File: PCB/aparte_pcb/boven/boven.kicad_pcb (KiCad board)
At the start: 2 copper layers, 100.5 x 100.5 mm, 48 parts, among them IC1 TSSP4038, IC10 TSSP4038, IC11 TSSP4038, IC12 TSSP4038, IC13 TSSP4038, IC14 TSSP4038, IC15 TSSP4038, IC16 TSSP4038, IC2 TSSP4038, IC3 TSSP4038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

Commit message: \x
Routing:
- net Net-(D2-A): track 350.8 -> 356.4 mm
- net Net-(D6-K): track 82.4 -> 83.5 mm
- net Net-(IC1-OUT): track 93.7 -> 93.0 mm

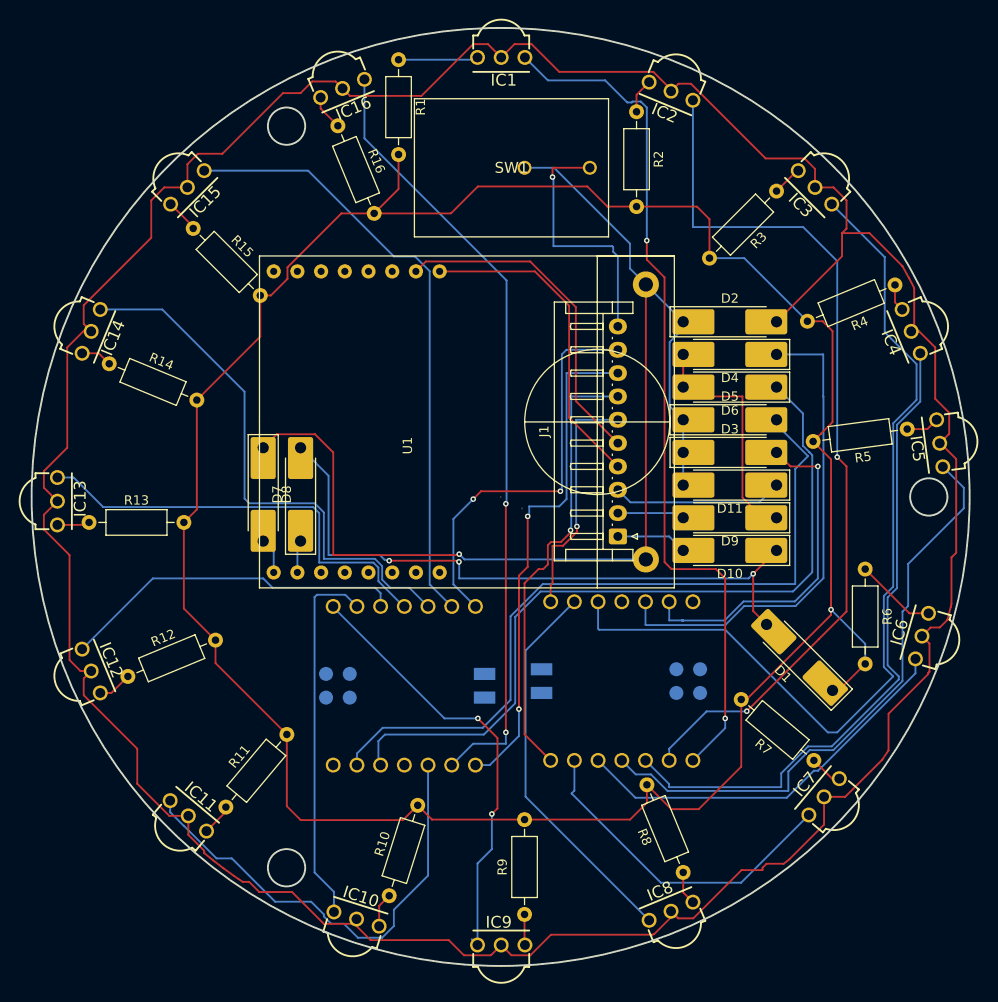
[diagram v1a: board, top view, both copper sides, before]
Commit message: schroef geaard
moet nog onderste schroef
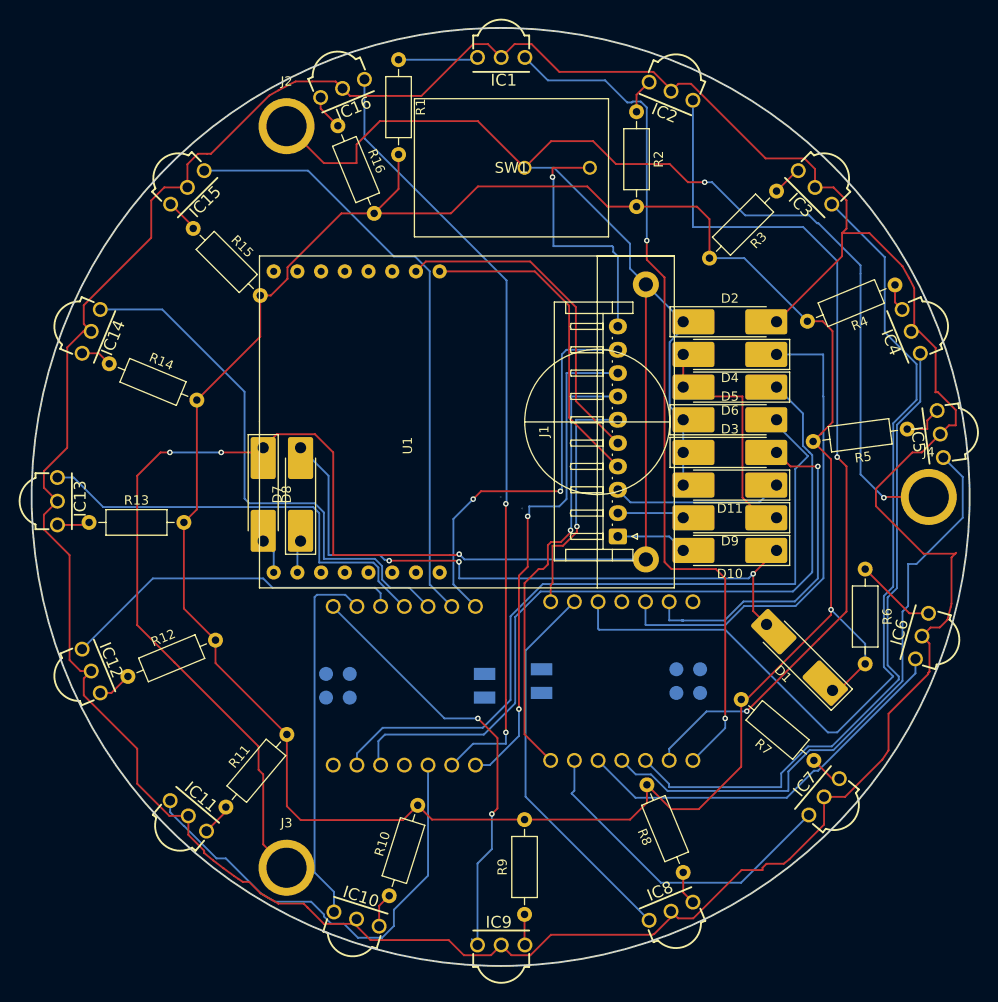
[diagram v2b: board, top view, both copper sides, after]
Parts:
- added J2: Screw_Terminal_01x01, Library:MountingHole_4.3mm_M4_ISO7380_Pad, F.Cu at (125.5, 53.0)
- added J3: Screw_Terminal_01x01, Library:MountingHole_4.3mm_M4_ISO7380_Pad, F.Cu at (125.5, 132.5)
- added J4: Screw_Terminal_01x01, Library:MountingHole_4.3mm_M4_ISO7380_Pad, F.Cu at (194.3, 92.8)
- moved IC5 0.99 mm to (194.0, 86.2)
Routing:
- net Net-(D11-A): track 127.2 -> 296.3 mm, vias 1 -> 5
- net Net-(D2-A): track 356.4 -> 365.5 mm
- net Net-(IC5-OUT): track 64.1 -> 65.5 mm
- net Net-(IC5-VS): track 3.57 -> 4.58 mm
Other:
- outline, holes or cut-outs redrawn

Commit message: dgsrf
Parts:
- SW1: footprint Library:R1966ABLKBLKEF -> Library:Rocker Switch 3-Pin, SPDT, 10A
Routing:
- net Net-(D11-A): track 296.3 -> 300.3 mm
- net Net-(D1-K): track 268.2 -> 266.4 mm
- net soft_power_sw: track 27.6 -> 26.8 mm

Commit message: ix
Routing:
- net Net-(D11-A): track 300.3 -> 301.2 mm
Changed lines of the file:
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@@
 		(fp_arc
 			(start 2.499999 3.9)
-			(mid -0.001153 5.603)
+			(mid -0.001154 5.603001)
 			(end -2.500844 3.897856)
 			(stroke
@@
 	)
 	(segment
-		(start 160.8 57.1)
-		(end 158.35 54.65)
-		(width 0.2)
-		(layer "F.Cu")
-		(net 4)
-	)
-	(segment
 		(start 135.5 52.5)
 		(end 149.55 52.5)
@@
 	)
 	(segment
-		(start 166.55 57.1)
-		(end 160.8 57.1)
-		(width 0.2)
-		(layer "F.Cu")
-		(net 4)
-	)
-	(segment
 		(start 124.45 86.05)
 		(end 128.55 86.05)
@@
 	)
 	(segment
-		(start 153.85 54.65)
-		(end 151 57.5)
+		(start 154.9 53.6)
+		(end 159.5 53.6)
 		(width 0.2)
 		(layer "F.Cu")
@@
 	)
 	(segment
-		(start 158.35 54.65)
-		(end 153.85 54.65)
+		(start 151 57.5)
+		(end 154.9 53.6)
 		(width 0.2)
 		(layer "F.Cu")
@@
 	)
 	(segment
+		(start 164.95 59.05)
+		(end 170.3 59.05)
+		(width 0.2)
+		(layer "F.Cu")
+		(net 4)
+	)
+	(segment
 		(start 125.5 132.5)
 		(end 123 130)
@@
 	)
 	(segment
-		(start 170.3 59.05)
-		(end 168.5 59.05)
-		(width 0.2)
-		(layer "F.Cu")
-		(net 4)
-	)
-	(segment
 		(start 127.48 54.98)
 		(end 129.5 57)
@@
 	)
 	(segment
-		(start 168.5 59.05)
-		(end 166.55 57.1)
+		(start 159.5 53.6)
+		(end 164.95 59.05)
 		(width 0.2)
 		(layer "F.Cu")
